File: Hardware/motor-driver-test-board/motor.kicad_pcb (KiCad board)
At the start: 2 copper layers, 8 parts, among them J1 Conn_01x11, J2 Conn_01x08, Q1 MMBF170, Q2 MMBF170, Q3 MMBF170, Q4 MMBF170, Q5 MMBF170, Q6 MMBF170

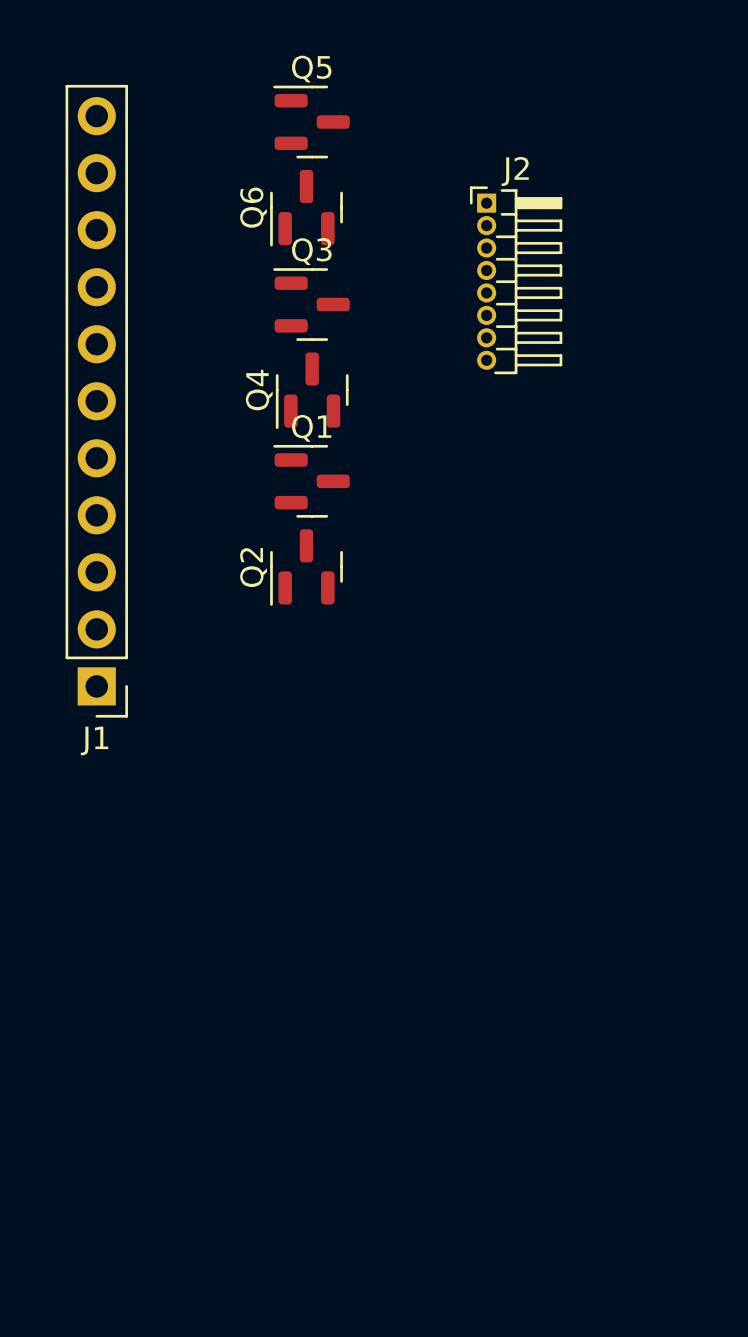
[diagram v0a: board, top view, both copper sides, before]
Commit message: layout initialised and redundant u v w signals taken away from J1
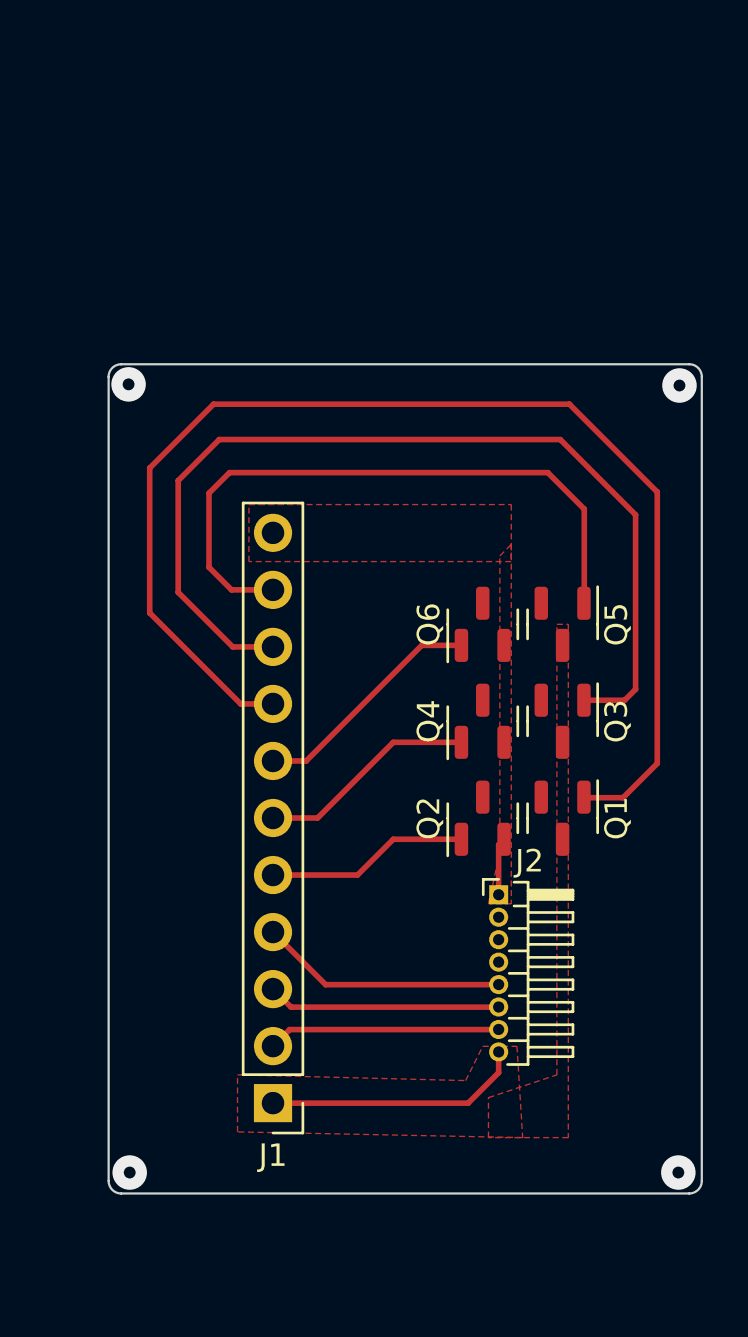
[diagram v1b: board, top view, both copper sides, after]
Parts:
- moved J2 30.8 mm to (144.7, 110.9)
- moved Q5 25.0 mm to (147.5, 98.8), turned to -90 degrees
- moved Q3 21.7 mm to (147.5, 103.1), turned to -90 degrees
- moved Q6 20.2 mm to (144.0, 98.8)
- moved J1 20.2 mm to (134.7, 120.2)
- moved Q1 18.7 mm to (147.5, 107.5), turned to -90 degrees
- moved Q4 16.6 mm to (144.0, 103.1)
- moved Q2 13.7 mm to (144.0, 107.5)
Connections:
- J1 pad 10: HALL_V -> WHS
- J1 pad 2: ULS -> HU
- J1 pad 3: UHS -> HV
- J1 pad 4: VLS -> HW
- J1 pad 5: VHS -> ULS
- J1 pad 6: WLS -> VLS
- J1 pad 7: WHS -> WLS
- J1 pad 8: HALL_U -> UHS
- J1 pad 9: HALL_V -> VHS
- J2 pad 1: VDD_Ctrl -> GND
- J2 pad 2: HALL_U -> W
- J2 pad 3: HALL_V -> V
- J2 pad 4: HALL_V -> U
- J2 pad 5: U -> HW
- J2 pad 6: V -> HV
- J2 pad 7: W -> HU
- J2 pad 8: GND -> VDD_Ctrl
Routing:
- net UHS: track 0.00 -> 55.0 mm
- net VHS: track 0.00 -> 43.0 mm
- net WHS: track 0.00 -> 28.5 mm
- net VDD_Ctrl: track 0.00 -> 11.5 mm
- net HW: track 0.00 -> 11.1 mm
- net WLS: track 0.00 -> 10.5 mm
- net HV: track 0.00 -> 10.4 mm
- net HU: track 0.00 -> 10.4 mm
- net VLS: track 0.00 -> 9.79 mm
- net ULS: track 0.00 -> 9.05 mm
- net GND: track 0.00 -> 2.57 mm
- net (no net): vias 0 -> 4
- added copper zone on F.Cu, net GND
- added copper zone on F.Cu, net VDD_Ctrl
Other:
- board outline added: 26.4 x 36.9 mm

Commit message: All connections completed on board & GND border added for testing convenience
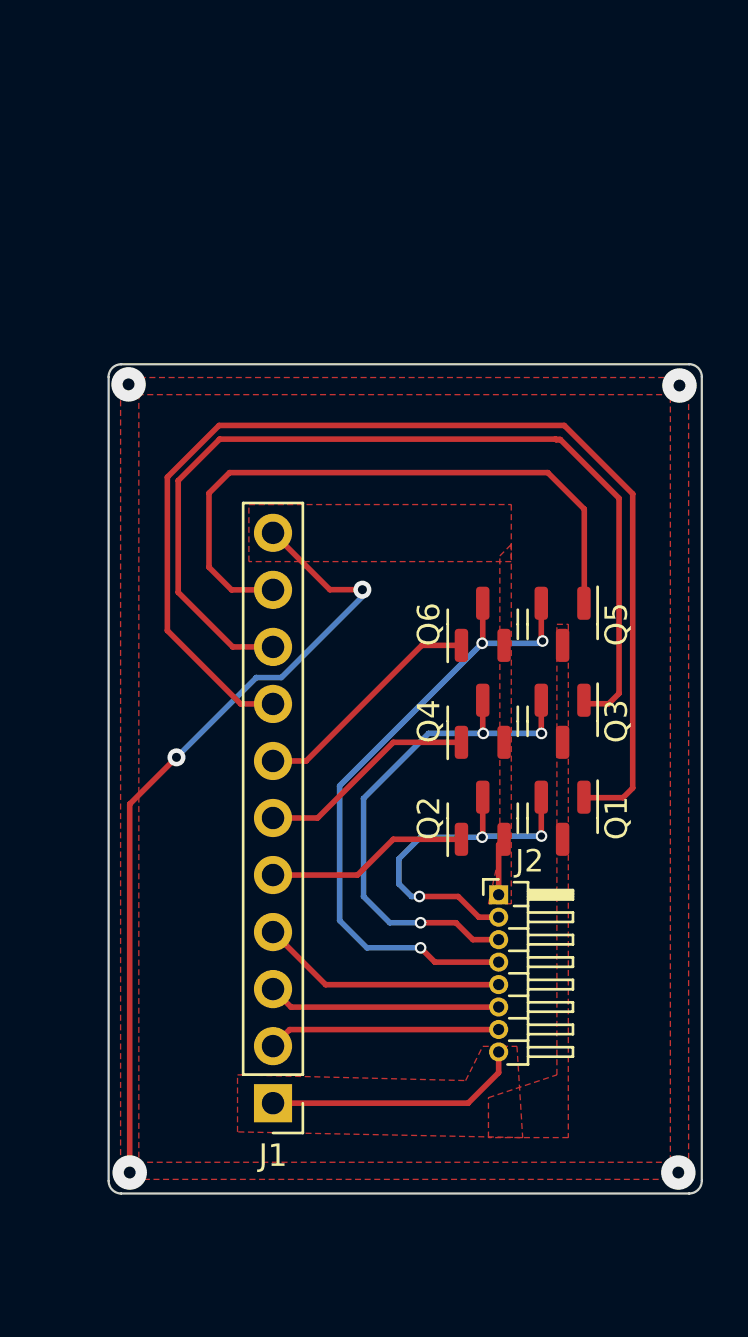
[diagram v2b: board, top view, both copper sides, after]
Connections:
- J2 pad 2: W -> U
- J2 pad 4: U -> W
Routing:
- net GND: track 2.57 -> 38.5 mm, vias 0 -> 6
- net W: track 0.00 -> 29.1 mm, vias 0 -> 3
- net V: track 0.00 -> 23.3 mm, vias 0 -> 3
- net U: track 0.00 -> 16.5 mm, vias 0 -> 3
- net UHS: track 55.0 -> 51.3 mm
- net VHS: track 43.0 -> 42.4 mm
- net (no net): vias 4 -> 0

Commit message: power polygons changed to trace, connector position shifted to the edge and boundary changed
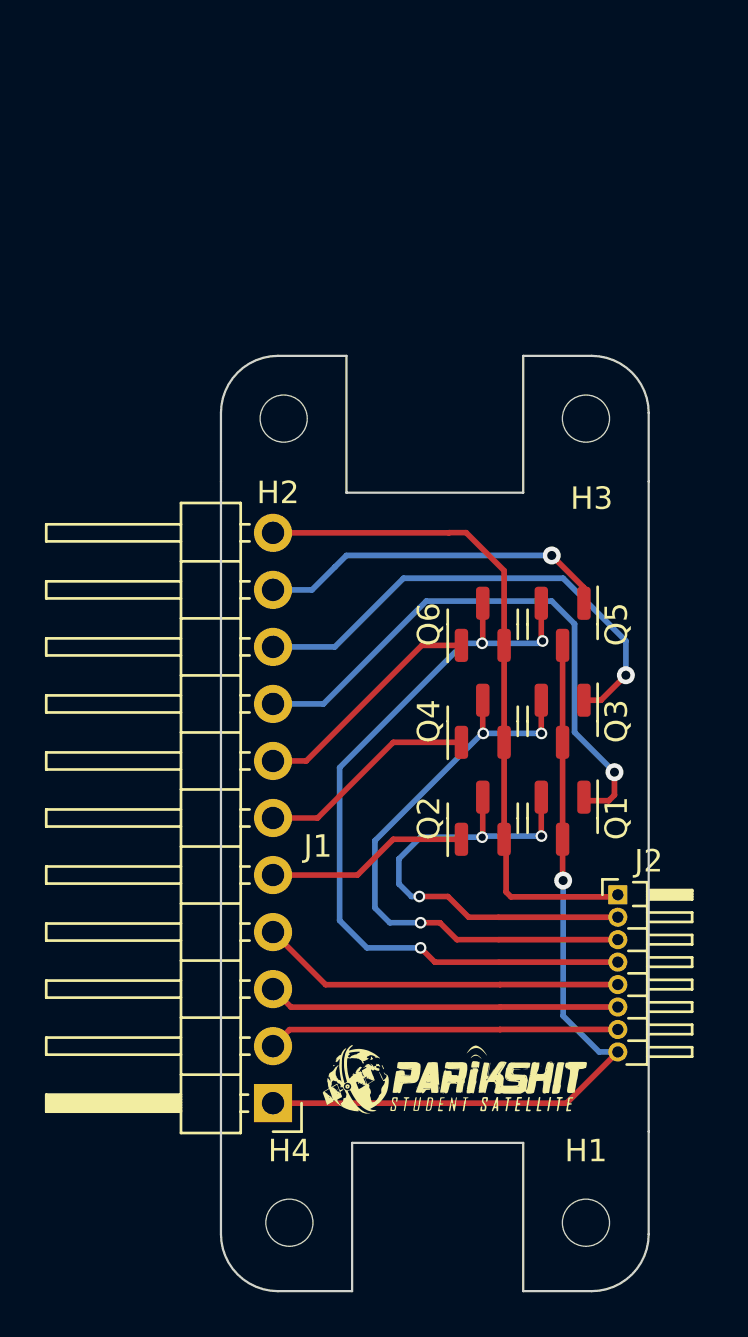
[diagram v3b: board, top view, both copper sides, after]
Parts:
- added G***: LOGO, motor-driver-test-board:parikshit_logo, F.Cu at (142.7, 119.1)
- added H1: MountingHole, MountingHole:MountingHole_2.1mm, F.Cu at (148.6, 125.5)
- added H2: MountingHole, MountingHole:MountingHole_2.1mm, F.Cu at (135.1, 89.7)
- added H3: MountingHole, MountingHole:MountingHole_2.1mm, F.Cu at (148.6, 89.7)
- added H4: MountingHole, MountingHole:MountingHole_2.1mm, F.Cu at (135.4, 125.5)
- J1: footprint Connector_PinHeader_2.54mm:PinHeader_1x11_P2.54mm_Vertical -> Connector_PinHeader_2.54mm:PinHeader_1x11_P2.54mm_Horizontal
- moved J2 5.31 mm to (150.0, 110.9)
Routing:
- net UHS: track 51.3 -> 25.7 mm, vias 0 -> 1
- net VDD_Ctrl: track 11.5 -> 35.9 mm, vias 0 -> 1
- net VHS: track 42.4 -> 22.0 mm, vias 0 -> 1
- net WHS: track 28.5 -> 15.8 mm, vias 0 -> 1
- net GND: track 38.5 -> 30.4 mm, vias 6 -> 0
- net W: track 29.1 -> 34.8 mm
- net U: track 16.5 -> 21.8 mm
- net HW: track 11.1 -> 16.3 mm
- net HU: track 10.4 -> 15.7 mm
- net HV: track 10.4 -> 15.7 mm
- net V: track 23.3 -> 26.8 mm
- removed copper zone on F.Cu, net GND
- removed copper zone on F.Cu, net VDD_Ctrl
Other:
- board size 26.4 x 36.9 mm -> 19 x 41.7 mm
